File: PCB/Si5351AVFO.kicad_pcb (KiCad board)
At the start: 4 copper layers, 100 x 65 mm, 133 parts, among them J1 USB_C_Receptacle, J2 SMA CLK0, J3 SMA CLK1, J4 SMA CLK2, J5 UPDI, SW1 EC11E18244A5, SW2 SOFT1, SW3 SOFT2, SW4 SOFT3, U1 LP2985-3.3, U2 Si5351A-B-GT, U3 CP2102N-A02-GQFN24, U4 ATtiny3226-SU, U5 LP2985-3.3, X1 25MHz TCXO

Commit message: Test points TP1-TP8 (GND x2, +5V, +3V3D, +3V3_CLK, +3V3_OLED, I2C_SCL/SDA) on B.Cu, 1.5 mm SMD, excluded from BOM/CPL; no RF nets. JLC fab outputs (tools/export_fab.sh -> PCB/production). ERC 0, DRC only the 15 accepted SMA edge hits
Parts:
- added TP1: GND, TestPoint:TestPoint_Pad_D1.5mm, B.Cu at (164.5, 102.8)
- added TP2: GND, TestPoint:TestPoint_Pad_D1.5mm, B.Cu at (124.0, 103.0)
- added TP3: +5V, TestPoint:TestPoint_Pad_D1.5mm, B.Cu at (106.9, 114.1)
- added TP4: +3V3D, TestPoint:TestPoint_Pad_D1.5mm, B.Cu at (176.1, 155.3)
- added TP5: +3V3_CLK, TestPoint:TestPoint_Pad_D1.5mm, B.Cu at (143.0, 101.8)
- added TP6: +3V3_OLED, TestPoint:TestPoint_Pad_D1.5mm, B.Cu at (119.9, 122.0)
- added TP7: I2C_SCL, TestPoint:TestPoint_Pad_D1.5mm, B.Cu at (167.0, 147.9)
- added TP8: I2C_SDA, TestPoint:TestPoint_Pad_D1.5mm, B.Cu at (163.3, 156.0)
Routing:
- net I2C_SCL: track 44.8 -> 47.1 mm
- net I2C_SDA: track 33.7 -> 35.4 mm
- net +5V: track 68.9 -> 70.7 mm, vias 0 -> 1
- net +3V3D: track 119.5 -> 121.3 mm
- net +3V3_CLK: track 66.0 -> 67.7 mm
- net +3V3_OLED: track 44.5 -> 46.2 mm

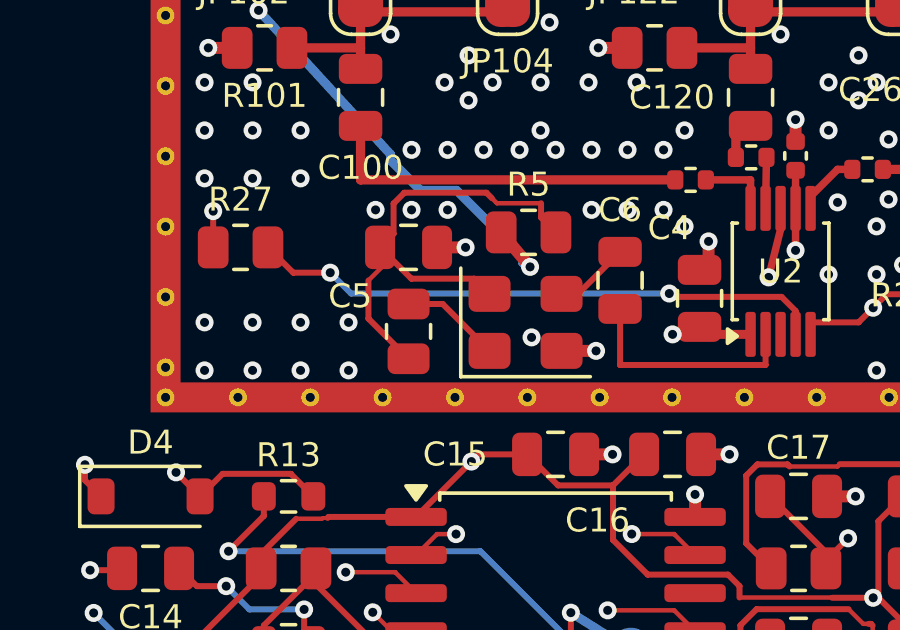
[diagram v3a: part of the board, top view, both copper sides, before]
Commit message: X1 TCXO pin 1 (NC/EN) tied to GND, R6 (VDD->pin 1) removed; same fix as OpenBeacon2 2de6f2e. PCB: R6 footprint and its VDD stub removed, X1.1 to GND via under X1, zones refilled. ERC 0, DRC 15 accepted SMA edge hits (unchanged), 0 unconnected/parity; docs + fab regenerated
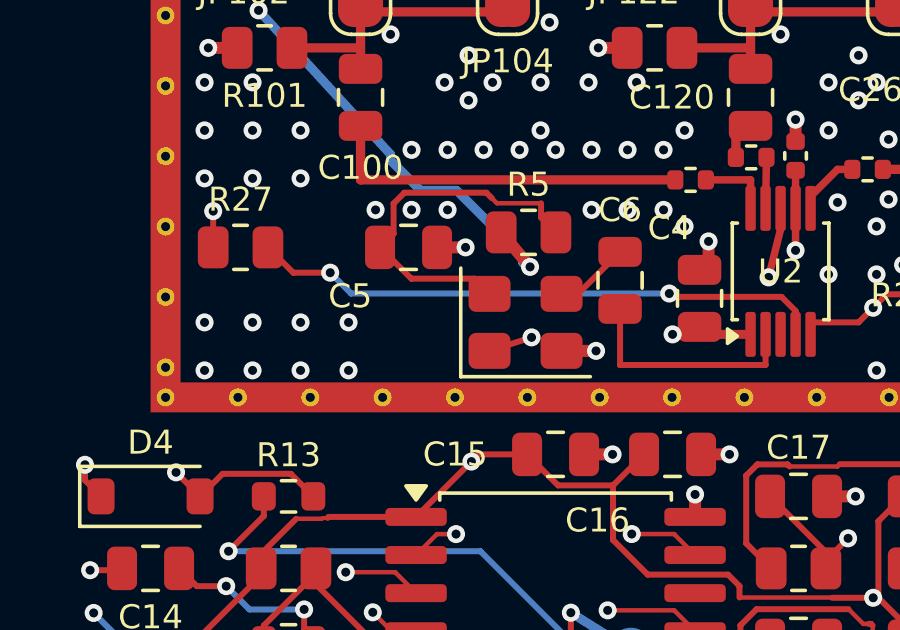
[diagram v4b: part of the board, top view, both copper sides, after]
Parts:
- removed R6: 0, Resistor_SMD:R_0805_2012Metric
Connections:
- X1 pad 1: Net-(X1-NC/EN) -> GND
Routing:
- net Net-(X1-VDD): track 16.5 -> 12.3 mm
- net Net-(X1-NC/EN): track 3.35 -> 0.00 mm
- net GND: track 67.2 -> 68.7 mm
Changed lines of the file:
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@@
 		)
 	)
-	(footprint "Resistor_SMD:R_0805_2012Metric"
-		(layer "F.Cu")
-		(at 159.6 137.3 90)
-		(descr "Resistor SMD 0805 (2012 Metric), square (rectangular) end terminal, IPC-7351 nominal, (Body size source: IPC-SM-782 page 72, https://www.pcb-3d.com/wordpress/wp-content/uploads/ipc-sm-782a_amendment_1_and_2.pdf)")
-		(tags "resistor")
-		(property "Reference" "R6"
-			(at 0 0 0)
-			(layer "F.Fab")
-			(effects
-				(font
-					(size 0.8 0.8)
-					(thickness 0.12)
-				)
-			)
-		)
-		(property "Value" "0"
-			(at 0 1.65 90)
-			(layer "F.Fab")
-			(hide yes)
-			(effects
-				(font
-					(size 1 1)
-					(thickness 0.15)
-				)
-			)
-		)
-		(property "Datasheet" ""
-			(at 0 0 90)
-			(layer "F.Fab")
-			(hide yes)
-			(effects
-				(font
-					(size 1.27 1.27)
-				)
-			)
-		)
-		(property "Description" "Resistor, small symbol"
-			(at 0 0 90)
-			(layer "F.Fab")
-			(hide yes)
-			(effects
-				(font
-					(size 1.27 1.27)
-				)
-			)
-		)
-		(property "KiLib_Generator" "SMD_2terminal_chip_molded"
-			(at 0 0 90)
-			(layer "F.SilkS")
-			(hide yes)
-			(effects
-				(font
-					(size 1 1)
-					(thickness 0.15)
-				)
-			)
-		)
-		(property "LCSC" "C17477"
-			(at 0 0 90)
-			(layer "F.SilkS")
-			(hide yes)
-			(effects
-				(font
-					(size 1.27 1.27)
-					(thickness 0.15)
-				)
-			)
-		)
-		(property "MPN" "0805W8F0000T5E"
-			(at 0 0 90)
-			(layer "F.SilkS")
-			(hide yes)
-			(effects
-				(font
-					(size 1.27 1.27)
-					(thickness 0.15)
-				)
-			)
-		)
-		(property "Manufacturer" "UNI-ROYAL"
-			(at 0 0 90)
-			(layer "F.SilkS")
-			(hide yes)
-			(effects
-				(font
-					(size 1.27 1.27)
-					(thickness 0.15)
-				)
-			)
-		)
-		(sheetname "Synth and RF outputs")
-		(sheetfile "synth_rf.kicad_sch")
-		(attr smd dnp)
-		(duplicate_pad_numbers_are_jumpers no)
-		(fp_line
-			(start -0.227064 -0.735)
-			(end 0.227064 -0.735)
-			(stroke
-				(width 0.12)
-				(type solid)
-			)
-			(layer "F.SilkS")
-		)
-		(fp_line
-			(start -0.227064 0.735)
-			(end 0.227064 0.735)
-			(stroke
-				(width 0.12)
-				(type solid)
-			)
-			(layer "F.SilkS")
-		)
-		(fp_rect
-			(start -1.68 -0.95)
-			(end 1.68 0.95)
-			(stroke
-				(width 0.05)
-				(type solid)
-			)
-			(fill no)
-			(layer "F.CrtYd")
-		)
-		(fp_rect
-			(start -1 -0.625)
-			(end 1 0.625)
-			(stroke
-				(width 0.1)
-				(type solid)
-			)
-			(fill no)
-			(layer "F.Fab")
-		)
-		(fp_text user "${REFERENCE}"
-			(at 0 0 90)
-			(layer "F.Fab")
-			(effects
-				(font
-					(size 0.5 0.5)
-					(thickness 0.08)
-				)
-			)
-		)
-		(pad "1" smd roundrect
-			(at -0.9125 0 90)
-			(size 1.025 1.4)
-			(layers "F.Cu" "F.Mask" "F.Paste")
-			(roundrect_rratio 0.243902)
-			(net "Net-(X1-VDD)")
-		)
-		(pad "2" smd roundrect
-			(at 0.9125 0 90)
-			(size 1.025 1.4)
-			(layers "F.Cu" "F.Mask" "F.Paste")
-			(roundrect_rratio 0.243902)
-			(net "Net-(X1-NC{slash}EN)")
-		)
-		(embedded_fonts no)
-		(model "${KICAD10_3DMODEL_DIR}/Resistor_SMD.3dshapes/R_0805_2012Metric.step"
-			(offset
-				(xyz 0 0 0)
-			)
-			(scale
-				(xyz 1 1 1)
-			)
-			(rotate
-				(xyz 0 0 0)
-			)
-		)
-	)
 	(footprint "Resistor_SMD:R_0603_1608Metric"
 		(layer "F.Cu")
@@
 			)
 		)
-		(property "Description" "4-pin 3225 TCXO, clipped-sine output; pin 1 NC/EN (NC on fitted part; EN on active-high-enable TCXOs via DNP R6)"
+		(property "Description" "4-pin 3225 TCXO, clipped-sine output; pin 1 NC/EN, tied to GND (YXC 3225 pin 1 is NC: float or GND)"
 			(at 0 0 0)
 			(layer "F.Fab")
@@
 			(layers "F.Cu" "F.Mask" "F.Paste")
 			(roundrect_rratio 0.208333)
-			(net "Net-(X1-NC{slash}EN)")
+			(net "GND")
 		)
 		(pad "2" smd roundrect
@@
 	)
 	(segment
+		(start 162.3 137.95)
+		(end 163.7 137.5)
+		(width 0.2)
+		(layer "F.Cu")
+		(net "GND")
+	)
+	(segment
 		(start 113.1 109.775)
 		(end 113.1 108.925)
@@
 	)
 	(segment
-		(start 162.5461 133.0288)
-		(end 162.3777 132.8604)
-		(width 0.15)
-		(layer "F.Cu")
-		(net "Net-(X1-VDD)")
-	)
-	(segment
-		(start 164.0168 133.0288)
-		(end 162.5461 133.0288)
-		(width 0.15)
-		(layer "F.Cu")
-		(net "Net-(X1-VDD)")
-	)
-	(segment
-		(start 159.1 134.05)
-		(end 158.65 134.5)
-		(width 0.2)
-		(layer "F.Cu")
-		(net "Net-(X1-VDD)")
-	)
-	(segment
-		(start 162.1948 132.6775)
-		(end 159.4616 132.6775)
-		(width 0.2)
-		(layer "F.Cu")
-		(net "Net-(X1-VDD)")
-	)
-	(segment
-		(start 164.5125 134)
-		(end 164.0168 133.5043)
-		(width 0.2)
-		(layer "F.Cu")
-		(net "Net-(X1-VDD)")
-	)
-	(segment
-		(start 159.1 133.0391)
-		(end 159.1 134.05)
-		(width 0.2)
-		(layer "F.Cu")
-		(net "Net-(X1-VDD)")
-	)
-	(segment
-		(start 162.3777 132.8604)
-		(end 162.1948 132.6775)
-		(width 0.2)
-		(layer "F.Cu")
-		(net "Net-(X1-VDD)")
-	)
-	(segment
-		(start 164.0168 133.5043)
-		(end 164.0168 133.0288)
-		(width 0.2)
-		(layer "F.Cu")
-		(net "Net-(X1-VDD)")
-	)
-	(segment
-		(start 158.2622 135.6038)
-		(end 159.008 134.858)
-		(width 0.15)
-		(layer "F.Cu")
-		(net "Net-(X1-VDD)")
-	)
-	(segment
-		(start 159.4616 132.6775)
-		(end 159.1 133.0391)
-		(width 0.2)
-		(layer "F.Cu")
-		(net "Net-(X1-VDD)")
-	)
-	(segment
-		(start 161.7927 135.5427)
-		(end 162.3 136.05)
-		(width 0.2)
-		(layer "F.Cu")
-		(net "Net-(X1-VDD)")
-	)
-	(segment
-		(start 158.2622 136.8747)
-		(end 158.2622 135.6038)
-		(width 0.2)
-		(layer "F.Cu")
-		(net "Net-(X1-VDD)")
-	)
-	(segment
-		(start 159.6927 135.5427)
-		(end 161.7927 135.5427)
-		(width 0.2)
-		(layer "F.Cu")
-		(net "Net-(X1-VDD)")
-	)
-	(segment
-		(start 159.6 138.2125)
-		(end 158.2622 136.8747)
-		(width 0.2)
-		(layer "F.Cu")
-		(net "Net-(X1-VDD)")
-	)
-	(segment
-		(start 158.65 134.5)
-		(end 159.008 134.858)
-		(width 0.2)
-		(layer "F.Cu")
-		(net "Net-(X1-VDD)")
-	)
-	(segment
-		(start 159.008 134.858)
-		(end 159.6927 135.5427)
-		(width 0.2)
-		(layer "F.Cu")
-		(net "Net-(X1-VDD)")
-	)
-	(segment
-		(start 160.7375 136.3875)
-		(end 162.3 137.95)
-		(width 0.2)
-		(layer "F.Cu")
-		(net "Net-(X1-NC{slash}EN)")
-	)
-	(segment
-		(start 159.6 136.3875)
-		(end 160.7375 136.3875)
-		(width 0.2)
-		(layer "F.Cu")
-		(net "Net-(X1-NC{slash}EN)")
-	)
-	(segment
 		(start 148.8133 142.2633)
 		(end 148.8133 141.7469)
@@
 	)
 	(segment
+		(start 162.5461 133.0288)
+		(end 162.3777 132.8604)
+		(width 0.15)
+		(layer "F.Cu")
+		(net "Net-(X1-VDD)")
+	)
+	(segment
+		(start 164.0168 133.0288)
+		(end 162.5461 133.0288)
+		(width 0.15)
+		(layer "F.Cu")
+		(net "Net-(X1-VDD)")
+	)
+	(segment
+		(start 159.1 134.05)
+		(end 158.65 134.5)
+		(width 0.2)
+		(layer "F.Cu")
+		(net "Net-(X1-VDD)")
+	)
+	(segment
+		(start 162.1948 132.6775)
+		(end 159.4616 132.6775)
+		(width 0.2)
+		(layer "F.Cu")
+		(net "Net-(X1-VDD)")
+	)
+	(segment
+		(start 164.5125 134)
+		(end 164.0168 133.5043)
+		(width 0.2)
+		(layer "F.Cu")
+		(net "Net-(X1-VDD)")
+	)
+	(segment
+		(start 159.1 133.0391)
+		(end 159.1 134.05)
+		(width 0.2)
+		(layer "F.Cu")
+		(net "Net-(X1-VDD)")
+	)
+	(segment
+		(start 162.3777 132.8604)
+		(end 162.1948 132.6775)
+		(width 0.2)
+		(layer "F.Cu")
+		(net "Net-(X1-VDD)")
+	)
+	(segment
+		(start 164.0168 133.5043)
+		(end 164.0168 133.0288)
+		(width 0.2)
+		(layer "F.Cu")
+		(net "Net-(X1-VDD)")
+	)
+	(segment
+		(start 159.4616 132.6775)
+		(end 159.1 133.0391)
+		(width 0.2)
+		(layer "F.Cu")
+		(net "Net-(X1-VDD)")
+	)
+	(segment
+		(start 161.7927 135.5427)
+		(end 162.3 136.05)
+		(width 0.2)
+		(layer "F.Cu")
+		(net "Net-(X1-VDD)")
+	)
+	(segment
+		(start 159.6927 135.5427)
+		(end 161.7927 135.5427)
+		(width 0.2)
+		(layer "F.Cu")
+		(net "Net-(X1-VDD)")
+	)
+	(segment
+		(start 158.65 134.5)
+		(end 159.008 134.858)
+		(width 0.2)
+		(layer "F.Cu")
+		(net "Net-(X1-VDD)")
+	)
+	(segment
+		(start 159.008 134.858)
+		(end 159.6927 135.5427)
+		(width 0.2)
+		(layer "F.Cu")
+		(net "Net-(X1-VDD)")
+	)
+	(segment
